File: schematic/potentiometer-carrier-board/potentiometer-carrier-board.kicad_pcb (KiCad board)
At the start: 2 copper layers, 45.7 x 40.6 mm, 3 parts, among them J1 Conn_01x05, J2 Conn_01x05, J3 Conn_01x03_Socket

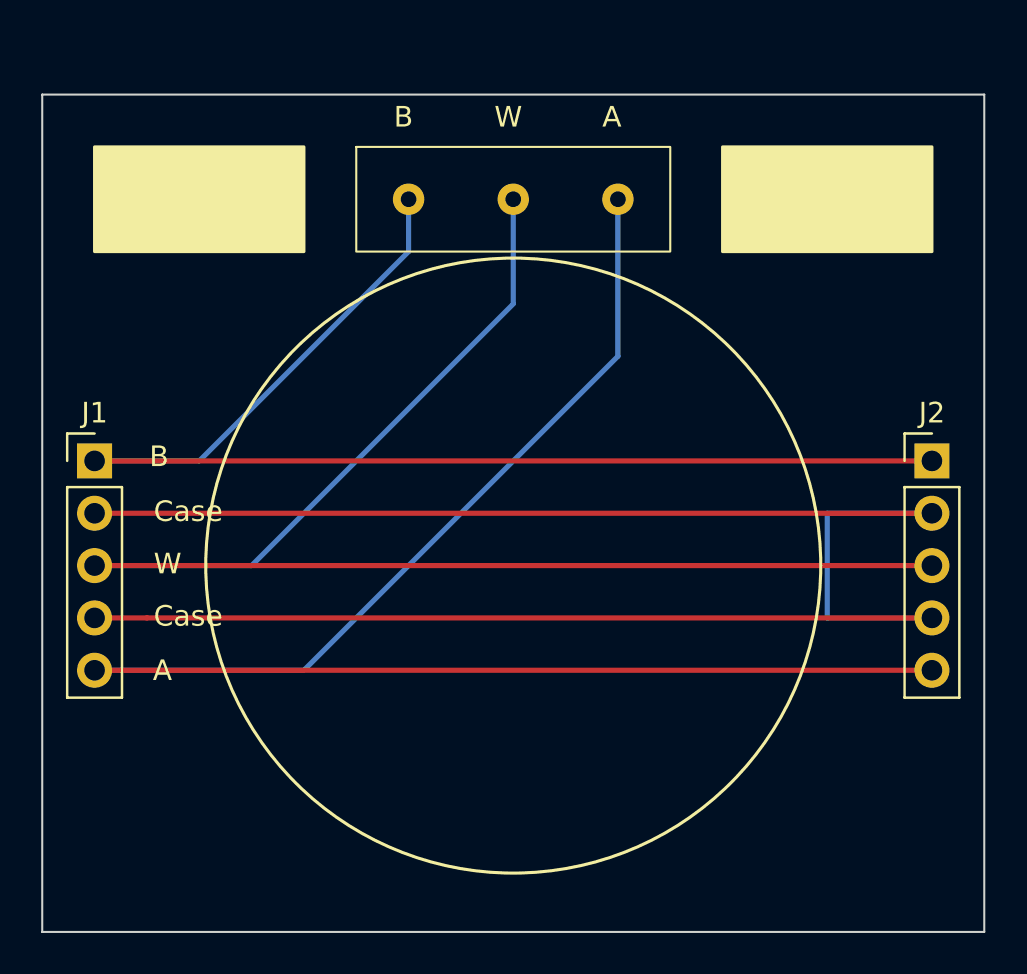
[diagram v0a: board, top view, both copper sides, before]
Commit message: Minor changes to tighten the fit.
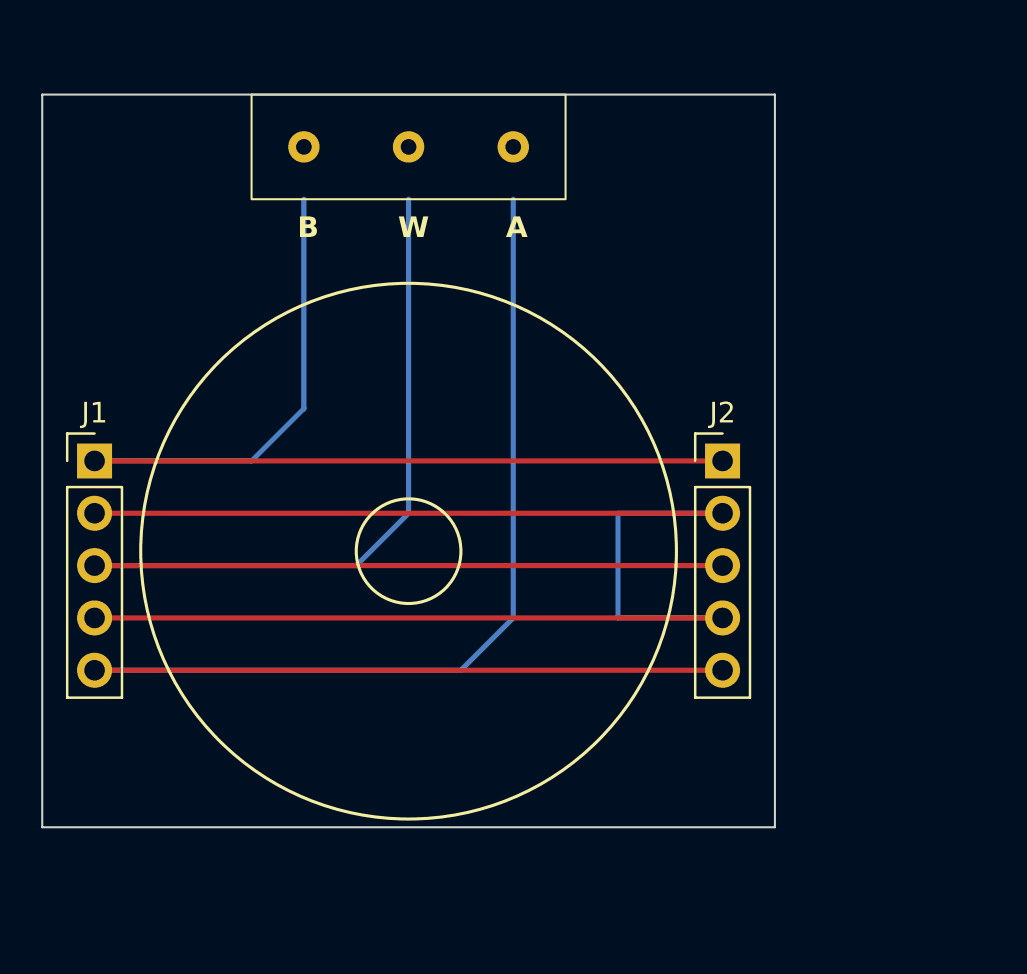
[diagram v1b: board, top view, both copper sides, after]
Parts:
- moved J2 10.2 mm to (78.7, 63.5)
- moved J3 5.68 mm to (63.5, 45.7)
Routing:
- net Net-(J1-Pin_2): track 96.5 -> 75.9 mm
- net Net-(J1-Pin_1): track 62.6 -> 51.7 mm
- net Net-(J1-Pin_3): track 71.3 -> 61.9 mm
- net Net-(J1-Pin_5): track 80.0 -> 72.0 mm
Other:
- board size 45.7 x 40.6 mm -> 35.6 x 35.6 mm
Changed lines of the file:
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@@
         (effects (font (size 1 1) (thickness 0.15)))
     )
-    (fp_text value "Conn_01x05" (at 0 12.49) (layer "F.Fab")
+    (fp_text value "Conn_01x05" (at 0 12.49) (layer "F.Fab") hide
         (effects (font (size 1 1) (thickness 0.15)))
     )
@@
   )
   (footprint "Connector_PinHeader_2.54mm:PinHeader_1x05_P2.54mm_Vertical" (layer "F.Cu")
-    (at 88.9 63.5)
+    (at 78.74 63.5)
     (descr "Through hole straight pin header, 1x05, 2.54mm pitch, single row")
     (tags "Through hole pin header THT 1x05 2.54mm single row")
@@
         (effects (font (size 1 1) (thickness 0.15)))
     )
-    (fp_text value "Conn_01x05" (at 0 12.49) (layer "F.Fab")
+    (fp_text value "Conn_01x05" (at 0 12.49) (layer "F.Fab") hide
         (effects (font (size 1 1) (thickness 0.15)))
     )
@@
   )
   (footprint "Ivan Hawkes:Pads 01x03-5.08mm" (layer "F.Cu")
-    (at 68.58 48.26)
+    (at 63.5 45.72)
     (property "Sheetfile" "potentiometer-carrier-board.kicad_sch")
     (property "Sheetname" "")
@@
         (effects (font (size 1 1) (thickness 0.1)))
     )
-    (fp_text value "Conn_01x03_Socket" (at 0 2.54 unlocked) (layer "F.Fab")
+    (fp_text value "Conn_01x03_Socket" (at 0 2.54 unlocked) (layer "F.Fab") hide
         (effects (font (size 1 1) (thickness 0.15)))
     )
-    (fp_text user "B" (at -4.953252 -0.864816 unlocked) (layer "B.SilkS")
-        (effects (font (size 1 1) (thickness 0.1)) (justify left bottom mirror))
+    (fp_text user "B" (at -4.548839 7.035773 unlocked) (layer "B.SilkS")
+        (effects (font (size 1 1) (thickness 0.2) bold) (justify left bottom mirror))
     )
-    (fp_text user "W" (at 0.225109 -0.854333 unlocked) (layer "B.SilkS")
-        (effects (font (size 1 1) (thickness 0.1)) (justify left bottom mirror))
+    (fp_text user "W" (at 0.629522 7.046256 unlocked) (layer "B.SilkS")
+        (effects (font (size 1 1) (thickness 0.2) bold) (justify left bottom mirror))
     )
-    (fp_text user "A" (at 5.351059 -0.864816 unlocked) (layer "B.SilkS")
-        (effects (font (size 1 1) (thickness 0.1)) (justify left bottom mirror))
+    (fp_text user "A" (at 5.755472 7.035773 unlocked) (layer "B.SilkS")
+        (effects (font (size 1 1) (thickness 0.2) bold) (justify left bottom mirror))
     )
-    (fp_text user "B" (at -5.801027 -0.866125 unlocked) (layer "F.SilkS")
-        (effects (font (size 1 1) (thickness 0.1)) (justify left bottom))
+    (fp_text user "B" (at -5.396614 7.034464 unlocked) (layer "F.SilkS")
+        (effects (font (size 1 1) (thickness 0.2) bold) (justify left bottom))
     )
-    (fp_text user "W" (at -0.918796 -0.866125 unlocked) (layer "F.SilkS")
-        (effects (font (size 1 1) (thickness 0.1)) (justify left bottom))
+    (fp_text user "W" (at -0.514383 7.034464 unlocked) (layer "F.SilkS")
+        (effects (font (size 1 1) (thickness 0.2) bold) (justify left bottom))
     )
-    (fp_text user "A" (at 4.317219 -0.866125 unlocked) (layer "F.SilkS")
-        (effects (font (size 1 1) (thickness 0.1)) (justify left bottom))
+    (fp_text user "A" (at 4.721632 7.034464 unlocked) (layer "F.SilkS")
+        (effects (font (size 1 1) (thickness 0.2) bold) (justify left bottom))
     )
     (fp_rect (start -7.62 0) (end 7.62 5.08)
@@
       (net 4 "Net-(J1-Pin_5)") (pinfunction "Pin_3") (pintype "passive"))
   )
-  (gr_rect (start 78.74 48.26) (end 88.9 53.34)
-    (stroke (width 0.15) (type solid)) (fill solid) (layer "F.SilkS"))
-  (gr_circle (center 68.58 68.58) (end 77.837615 80.285677)
+  (gr_circle (center 63.5 67.88) (end 76.5 67.88)
     (stroke (width 0.15) (type default)) (fill none) (layer "F.SilkS"))
-  (gr_rect (start 48.26 48.26) (end 58.42 53.34)
-    (stroke (width 0.15) (type solid)) (fill solid) (layer "F.SilkS"))
-  (gr_rect (start 45.72 45.72) (end 91.44 86.36)
+  (gr_circle (center 63.5 67.88) (end 66.04 67.88)
+    (stroke (width 0.15) (type default)) (fill none) (layer "F.SilkS"))
+  (gr_rect (start 45.72 45.72) (end 81.28 81.28)
     (stroke (width 0.1) (type default)) (fill none) (layer "Edge.Cuts"))
   (gr_text "W" (at 52.259584 69.030218) (layer "B.SilkS")
     (effects (font (size 1 1) (thickness 0.15)) (justify left bottom mirror))
   )
-  (gr_text "Case" (at 55.495528 65.808343) (layer "B.SilkS")
+  (gr_text "Case" (at 54.736501 66.406555) (layer "B.SilkS")
     (effects (font (size 1 1) (thickness 0.15)) (justify left bottom mirror))
   )
@@
     (effects (font (size 1 1) (thickness 0.15)) (justify left bottom mirror))
   )
-  (gr_text "Case" (at 55.495528 70.888343) (layer "B.SilkS")
+  (gr_text "Case" (at 54.736501 71.511458) (layer "B.SilkS")
     (effects (font (size 1 1) (thickness 0.15)) (justify left bottom mirror))
   )
@@
     (effects (font (size 1 1) (thickness 0.15)) (justify left bottom mirror))
   )
-  (gr_text "Case" (at 51.127491 66.537999) (layer "F.SilkS")
-    (effects (font (size 1 1) (thickness 0.15)) (justify left bottom))
-  )
-  (gr_text "W" (at 51.127491 69.077999) (layer "F.SilkS")
-    (effects (font (size 1 1) (thickness 0.15)) (justify left bottom))
-  )
-  (gr_text "B" (at 50.916451 63.872349) (layer "F.SilkS")
-    (effects (font (size 1 1) (thickness 0.15)) (justify left bottom))
-  )
-  (gr_text "Case" (at 51.127491 71.617999) (layer "F.SilkS")
-    (effects (font (size 1 1) (thickness 0.15)) (justify left bottom))
-  )
-  (gr_text "A" (at 51.085283 74.25551) (layer "F.SilkS")
-    (effects (font (size 1 1) (thickness 0.15)) (justify left bottom))
-  )
-  (segment (start 88.9 63.5) (end 48.26 63.5) (width 0.25) (layer "F.Cu") (net 1))
-  (segment (start 48.26 63.5) (end 53.34 63.5) (width 0.25) (layer "B.Cu") (net 1))
-  (segment (start 53.34 63.5) (end 63.5 53.34) (width 0.25) (layer "B.Cu") (net 1))
-  (segment (start 63.5 53.34) (end 63.5 50.8) (width 0.25) (layer "B.Cu") (net 1))
-  (segment (start 48.26 66.04) (end 88.9 66.04) (width 0.25) (layer "F.Cu") (net 2))
-  (segment (start 50.8 71.12) (end 88.9 71.12) (width 0.25) (layer "F.Cu") (net 2))
-  (segment (start 50.8 71.12) (end 48.26 71.12) (width 0.25) (layer "F.Cu") (net 2))
-  (segment (start 83.82 71.12) (end 88.9 71.12) (width 0.25) (layer "B.Cu") (net 2))
-  (segment (start 83.82 66.04) (end 83.82 71.12) (width 0.25) (layer "B.Cu") (net 2))
-  (segment (start 88.9 66.04) (end 83.82 66.04) (width 0.25) (layer "B.Cu") (net 2))
-  (segment (start 48.26 68.58) (end 88.9 68.58) (width 0.25) (layer "F.Cu") (net 3))
-  (segment (start 68.58 55.88) (end 68.58 50.8) (width 0.25) (layer "B.Cu") (net 3))
-  (segment (start 55.88 68.58) (end 68.58 55.88) (width 0.25) (layer "B.Cu") (net 3))
-  (segment (start 48.26 68.58) (end 55.88 68.58) (width 0.25) (layer "B.Cu") (net 3))
-  (segment (start 88.9 73.66) (end 48.26 73.66) (width 0.25) (layer "F.Cu") (net 4))
-  (segment (start 48.26 73.66) (end 58.42 73.66) (width 0.25) (layer "B.Cu") (net 4))
-  (segment (start 73.66 58.42) (end 73.66 50.8) (width 0.25) (layer "B.Cu") (net 4))
-  (segment (start 58.42 73.66) (end 73.66 58.42) (width 0.25) (layer "B.Cu") (net 4))
+  (segment (start 48.26 63.5) (end 78.615 63.5) (width 0.25) (layer "F.Cu") (net 1))
+  (segment (start 58.42 60.96) (end 58.42 50.8) (width 0.25) (layer "B.Cu") (net 1))
+  (segment (start 48.26 63.5) (end 55.88 63.5) (width 0.25) (layer "B.Cu") (net 1))
+  (segment (start 55.88 63.5) (end 58.42 60.96) (width 0.25) (layer "B.Cu") (net 1))
+  (segment (start 48.26 71.12) (end 78.615 71.12) (width 0.25) (layer "F.Cu") (net 2))
+  (segment (start 48.26 66.04) (end 78.615 66.04) (width 0.25) (layer "F.Cu") (net 2))
+  (segment (start 73.66 71.12) (end 78.74 71.12) (width 0.25) (layer "B.Cu") (net 2))
+  (segment (start 73.66 66.04) (end 73.66 71.12) (width 0.25) (layer "B.Cu") (net 2))
+  (segment (start 78.74 66.04) (end 73.66 66.04) (width 0.25) (layer "B.Cu") (net 2))
+  (segment (start 48.26 68.58) (end 78.615 68.58) (width 0.25) (layer "F.Cu") (net 3))
+  (segment (start 60.96 68.58) (end 63.5 66.04) (width 0.25) (layer "B.Cu") (net 3))
+  (segment (start 63.5 66.04) (end 63.5 50.8) (width 0.25) (layer "B.Cu") (net 3))
+  (segment (start 48.26 68.58) (end 60.96 68.58) (width 0.25) (layer "B.Cu") (net 3))
+  (segment (start 48.26 73.66) (end 78.615 73.66) (width 0.25) (layer "F.Cu") (net 4))
+  (segment (start 66.04 73.66) (end 68.58 71.12) (width 0.25) (layer "B.Cu") (net 4))
+  (segment (start 68.58 71.12) (end 68.58 50.8) (width 0.25) (layer "B.Cu") (net 4))
+  (segment (start 48.26 73.66) (end 66.04 73.66) (width 0.25) (layer "B.Cu") (net 4))
 )

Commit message: Made the board slightly longer to stop the top box from being cropped. Exported gerbers and drill files.
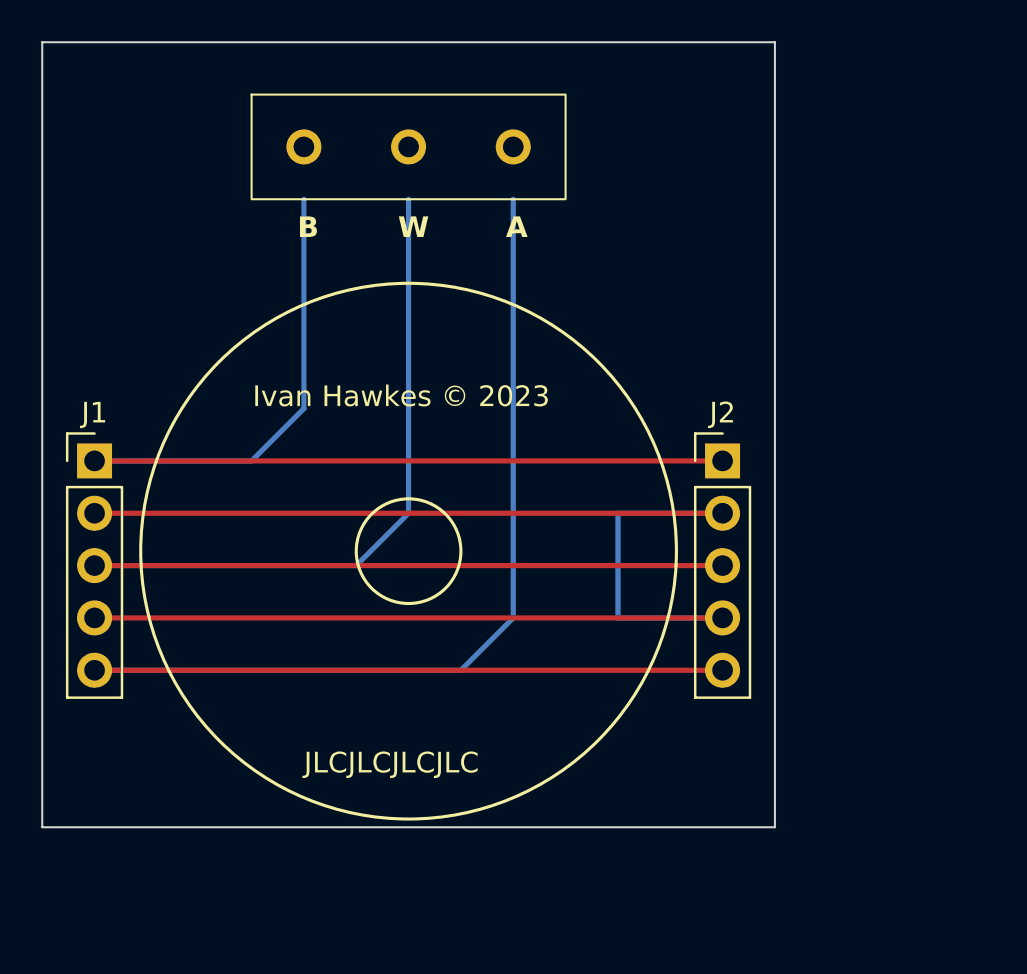
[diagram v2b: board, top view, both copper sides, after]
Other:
- board size 35.6 x 35.6 mm -> 35.6 x 38.1 mm
- board text added: "Ivan Hawkes © 2023"
- board text added: "JLCJLCJLCJLC"
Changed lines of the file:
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@@
       (plot_on_all_layers_selection 0x0000000_00000000)
       (disableapertmacros false)
-      (usegerberextensions false)
+      (usegerberextensions true)
       (usegerberattributes true)
       (usegerberadvancedattributes true)
@@
       (plotinvisibletext false)
       (sketchpadsonfab false)
-      (subtractmaskfromsilk false)
+      (subtractmaskfromsilk true)
       (outputformat 1)
       (mirror false)
-      (drillshape 1)
+      (drillshape 0)
       (scaleselection 1)
-      (outputdirectory "")
+      (outputdirectory "plots/")
     )
   )
@@
     (fp_rect (start -7.62 0) (end 7.62 5.08)
       (stroke (width 0.1) (type default)) (fill none) (layer "F.SilkS"))
-    (pad "1" thru_hole circle (at -5.08 2.54) (size 1.524 1.524) (drill 0.762) (layers "*.Cu" "*.Mask")
+    (pad "1" thru_hole circle (at -5.08 2.54) (size 1.7 1.7) (drill 1) (layers "*.Cu" "*.Mask")
       (net 1 "Net-(J1-Pin_1)") (pinfunction "Pin_1") (pintype "passive"))
-    (pad "2" thru_hole circle (at 0 2.54) (size 1.524 1.524) (drill 0.762) (layers "*.Cu" "*.Mask")
+    (pad "2" thru_hole circle (at 0 2.54) (size 1.7 1.7) (drill 1) (layers "*.Cu" "*.Mask")
       (net 3 "Net-(J1-Pin_3)") (pinfunction "Pin_2") (pintype "passive"))
-    (pad "3" thru_hole circle (at 5.08 2.54) (size 1.524 1.524) (drill 0.762) (layers "*.Cu" "*.Mask")
+    (pad "3" thru_hole circle (at 5.08 2.54) (size 1.7 1.7) (drill 1) (layers "*.Cu" "*.Mask")
       (net 4 "Net-(J1-Pin_5)") (pinfunction "Pin_3") (pintype "passive"))
   )
@@
   (gr_circle (center 63.5 67.88) (end 66.04 67.88)
     (stroke (width 0.15) (type default)) (fill none) (layer "F.SilkS"))
-  (gr_rect (start 45.72 45.72) (end 81.28 81.28)
+  (gr_rect (start 45.72 43.18) (end 81.28 81.28)
     (stroke (width 0.1) (type default)) (fill none) (layer "Edge.Cuts"))
   (gr_text "W" (at 52.259584 69.030218) (layer "B.SilkS")
@@
     (effects (font (size 1 1) (thickness 0.15)) (justify left bottom mirror))
   )
+  (gr_text "JLCJLCJLCJLC" (at 58.42 78.74) (layer "F.SilkS")
+    (effects (font (size 1 1) (thickness 0.15)) (justify left bottom))
+  )
+  (gr_text "Ivan Hawkes © 2023" (at 55.924093 60.96) (layer "F.SilkS")
+    (effects (font (size 1 1) (thickness 0.15)) (justify left bottom))
+  )
   (segment (start 48.26 63.5) (end 78.615 63.5) (width 0.25) (layer "F.Cu") (net 1))

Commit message: Made a footprint for the carrier boards. Test placed it on the PCB.
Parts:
- J1, J2: footprint Connector_PinHeader_2.54mm:PinHeader_1x05_P2.54mm_Vertical -> Ivan Hawkes:PinHeader_1x05_P2.54mm_Vertical
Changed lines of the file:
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@@
   (net 3 "Net-(J1-Pin_3)")
   (net 4 "Net-(J1-Pin_5)")
-  (footprint "Connector_PinHeader_2.54mm:PinHeader_1x05_P2.54mm_Vertical" (layer "F.Cu")
+  (footprint "Ivan Hawkes:PinHeader_1x05_P2.54mm_Vertical" (layer "F.Cu")
     (at 48.26 63.5)
     (descr "Through hole straight pin header, 1x05, 2.54mm pitch, single row")
@@
     )
   )
-  (footprint "Connector_PinHeader_2.54mm:PinHeader_1x05_P2.54mm_Vertical" (layer "F.Cu")
+  (footprint "Ivan Hawkes:PinHeader_1x05_P2.54mm_Vertical" (layer "F.Cu")
     (at 78.74 63.5)
     (descr "Through hole straight pin header, 1x05, 2.54mm pitch, single row")
